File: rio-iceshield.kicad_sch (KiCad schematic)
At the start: 66 parts, among them J2 Conn_01x06, J3 Conn_01x06, J4 Conn_01x06, J5 Conn_01x06, J6 Conn_01x06, J7 Conn_02x06_Odd_Even, U1 ICE40UP5K-SG48ITR, U2 AT25SF041B-SHD 4 Mb, U3 LD3985M122R_SOT23, U9 ULN2803A, X2 XO91, j1 GPIO

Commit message: WIP
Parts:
- C1, C3: footprint Capacitor_SMD:C_0805_2012Metric_Pad1.18x1.45mm_HandSolder -> Capacitor_SMD:C_0603_1608Metric_Pad1.08x0.95mm_HandSolder; LCSC PN (none) -> C19666
- C10, C14, C16, C18, C4, C5, C6, C7, C8, C9: footprint Capacitor_SMD:C_0805_2012Metric_Pad1.18x1.45mm_HandSolder -> Capacitor_SMD:C_0603_1608Metric_Pad1.08x0.95mm_HandSolder; LCSC PN (none) -> C14663
- C11: footprint Capacitor_SMD:C_0805_2012Metric_Pad1.18x1.45mm_HandSolder -> Capacitor_SMD:C_0603_1608Metric_Pad1.08x0.95mm_HandSolder; LCSC PN (none) -> C15525
- C12, C15: footprint Capacitor_SMD:C_0805_2012Metric_Pad1.18x1.45mm_HandSolder -> Capacitor_SMD:C_0603_1608Metric_Pad1.08x0.95mm_HandSolder; LCSC PN (none) -> C15849
- C13, C17, C2: footprint Capacitor_SMD:C_0805_2012Metric_Pad1.18x1.45mm_HandSolder -> Capacitor_SMD:C_0603_1608Metric_Pad1.08x0.95mm_HandSolder; LCSC PN (none) -> C57112
- D1: value 1N 4148WT7 DII -> 1N4148WS; footprint Diode_SMD:D_0603_1608Metric -> Diode_SMD:D_SOD-123; LCSC PN (none) -> C2128
- D2: LCSC PN (none) -> C2297
- D3: LCSC PN (none) -> C2296
- R1: footprint Resistor_SMD:R_0805_2012Metric_Pad1.20x1.40mm_HandSolder -> Resistor_SMD:R_0603_1608Metric_Pad0.98x0.95mm_HandSolder; LCSC PN (none) -> C22775
- R10, R11: value 900 -> 1k; footprint Resistor_SMD:R_0805_2012Metric_Pad1.20x1.40mm_HandSolder -> Resistor_SMD:R_0603_1608Metric_Pad0.98x0.95mm_HandSolder; LCSC PN (none) -> C21190
- R12: footprint Resistor_SMD:R_0805_2012Metric_Pad1.20x1.40mm_HandSolder -> Resistor_SMD:R_0603_1608Metric_Pad0.98x0.95mm_HandSolder; LCSC PN (none) -> C25804
- R13, R14, R15, R16, R17, R18, R19, R20, R21, R22, R23, R24, R25, R26, R27: footprint Resistor_SMD:R_0805_2012Metric_Pad1.20x1.40mm_HandSolder -> Resistor_SMD:R_0603_1608Metric_Pad0.98x0.95mm_HandSolder; LCSC PN (none) -> C4184
- R31, R32: footprint Resistor_SMD:R_0805_2012Metric_Pad1.20x1.40mm_HandSolder -> Resistor_SMD:R_0603_1608Metric_Pad0.98x0.95mm_HandSolder; LCSC PN (none) -> C22978
- R5: footprint Resistor_SMD:R_1206_3216Metric -> Resistor_SMD:R_0603_1608Metric_Pad0.98x0.95mm_HandSolder; LCSC PN (none) -> C4184
- U1: LCSC PN (none) -> C2678152
- U2: LCSC PN (none) -> C7457667
- U3: LCSC PN (none) -> C18199516
- U9: footprint Package_SO:SOIC-18W_7.5x11.6mm_P1.27mm -> Package_SO:SOP-18_7.495x11.515mm_P1.27mm; LCSC PN (none) -> C845537

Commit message: wip
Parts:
- removed J7: Conn_02x06_Odd_Even, Connector_PinHeader_2.54mm:PinHeader_2x06_P2.54mm_Vertical, symbol Connector_Generic:Conn_02x06_Odd_Even
- added TP10, TP11, TP12, TP13, TP2, TP3, TP4, TP5, TP6, TP7, TP8, TP9: TestPoint_Small, TestPoint:TestPoint_Pad_2.0x2.0mm, symbol Connector:TestPoint_Small
- renumbered R5 to R3, U9 to U10, input1 to input2, input0 to input2
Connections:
- net +3V3: now also TP12.1, TP13.1
- net 20: now also TP5.1
- net 21: now also TP4.1
- net 23: now also TP6.1
- net 25: now also TP3.1
- net 26: now also TP7.1
- net 27: now also TP2.1
- net 28: now also TP8.1
- net 31: now also TP10.1
- net GND: now also TP11.1, TP9.1

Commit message: wip
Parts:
- removed C18: 100n, Capacitor_SMD:C_0603_1608Metric_Pad1.08x0.95mm_HandSolder, symbol Device:C
- removed JP1, JP2: SolderJumper_3_Open, Jumper:SolderJumper-3_P1.3mm_Open_Pad1.0x1.5mm, symbol Jumper:SolderJumper_3_Open
- removed TP10, TP11, TP12, TP13, TP2, TP3, TP4, TP5, TP6, TP7, TP8, TP9: TestPoint_Small, TestPoint:TestPoint_Pad_2.0x2.0mm, symbol Connector:TestPoint_Small
- removed U3: LD3985M122R_SOT23, Package_TO_SOT_SMD:SOT-23-5, symbol Regulator_Linear:LD3985M122R_SOT23
- removed X2: XO91, Oscillator:Oscillator_SMD_EuroQuartz_XO91-4Pin_7.0x5.0mm, symbol Oscillator:XO91
- added R33, R34, R35, R36, R37: 1k2, Resistor_SMD:R_0603_1608Metric_Pad0.98x0.95mm_HandSolder, symbol Device:R
- added U7: LM317LD13TR, Package_SO:SOIC-8_3.9x4.9mm_P1.27mm, symbol Regulator_Linear:LM317L_SO8
- +24V-1, J2, J3, J4, J5, J6, Jo1, input2, j1: now not fitted; now left out of the parts list
- D1: footprint Diode_SMD:D_SOD-123 -> Diode_SMD:D_SOD-323_HandSoldering
- U2: footprint Package_SO:SOIC-8W_5.3x5.3mm_P1.27mm -> Package_SO:SOIC-8_3.9x4.9mm_P1.27mm; LCSC PN C7457667 -> C5127618
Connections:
- net +3V3: no longer C1.1
- net +5V: now also C1.1, U7.1 (VI)
- net 1v2: now also C2.1, R33.2, R34.2, R35.2, R36.2, R37.2, U7.2 (VO), U7.3 (VO), U7.6 (VO), U7.7 (VO)
- net GND: now also R33.1, R34.1, R35.1, R36.1, R37.1, U7.4 (ADJ)
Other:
- moved on the sheet: C2, C3

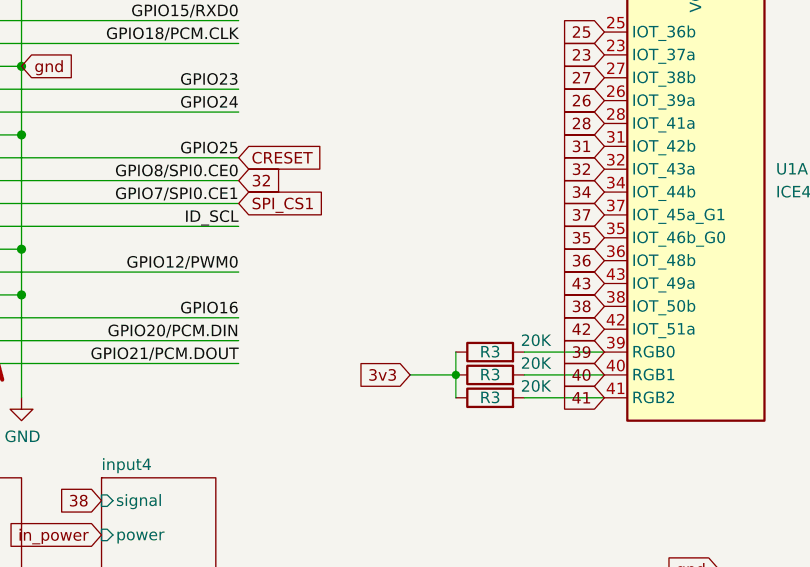
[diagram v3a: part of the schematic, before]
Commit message: Fix missing clk line
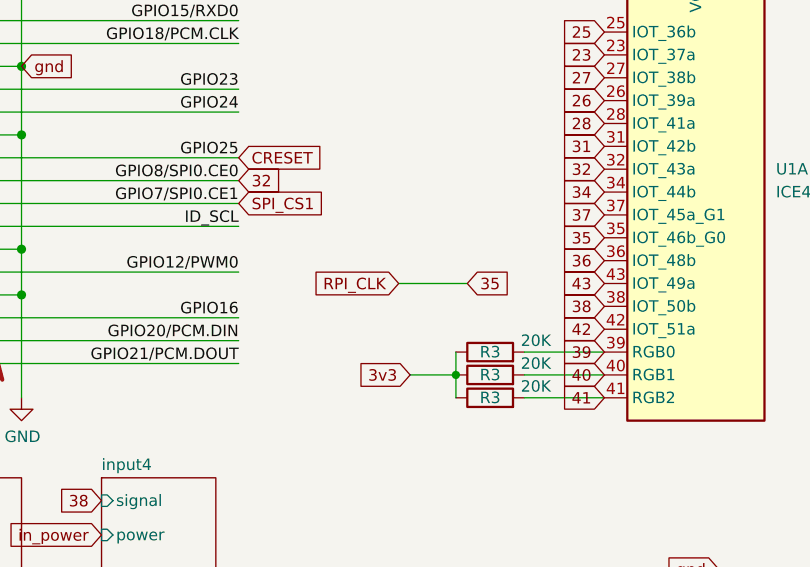
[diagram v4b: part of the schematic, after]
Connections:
- net RPI_CLK is gone; now on net 35: j1.7 (Pin_7)
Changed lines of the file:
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@@
+	(wire
+		(pts
+			(xy 125.73 67.31) (xy 118.11 67.31)
+		)
+		(stroke
+			(width 0)
+			(type default)
+		)
+	)
 	(wire
 		(pts
@@
 		)
 	)
+	(global_label "RPI_CLK"
+		(shape input)
+		(at 118.11 67.31 180)
+		(fields_autoplaced yes)
+		(effects
+			(font
+				(size 1.27 1.27)
+			)
+			(justify right)
+		)
+		(property "Intersheetrefs" "${INTERSHEET_REFS}"
+			(at 107.4286 67.31 0)
+			(effects
+				(font
+					(size 1.27 1.27)
+				)
+				(justify right)
+				(hide yes)
+			)
+		)
+	)
 	(global_label "12"
 		(shape input)
@@
 				(hide yes)
 			)
+		)
+	)
+	(global_label "35"
+		(shape input)
+		(at 125.73 67.31 0)
+		(fields_autoplaced yes)
+		(effects
+			(font
+				(size 1.27 1.27)
+			)
+			(justify left)
+		)
+		(property "Intersheetrefs" "${INTERSHEET_REFS}"
+			(at 131.2293 67.31 0)
+			(effects
+				(font
+					(size 1.27 1.27)
+				)
+				(justify left)
+				(hide yes)
+			)
